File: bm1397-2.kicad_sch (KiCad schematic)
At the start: 101 parts, among them IC1 BM1397_mode1, J3 Conn_01x05, U3 SN74LVC1T45DBVR, U5 MCP1824T-1802E, U5 SN74LVC1T45DBVR, U6 MCP1824T-0802E, U8 SN74LVC1T45DBVR, X1 OT322525MJBA4SL

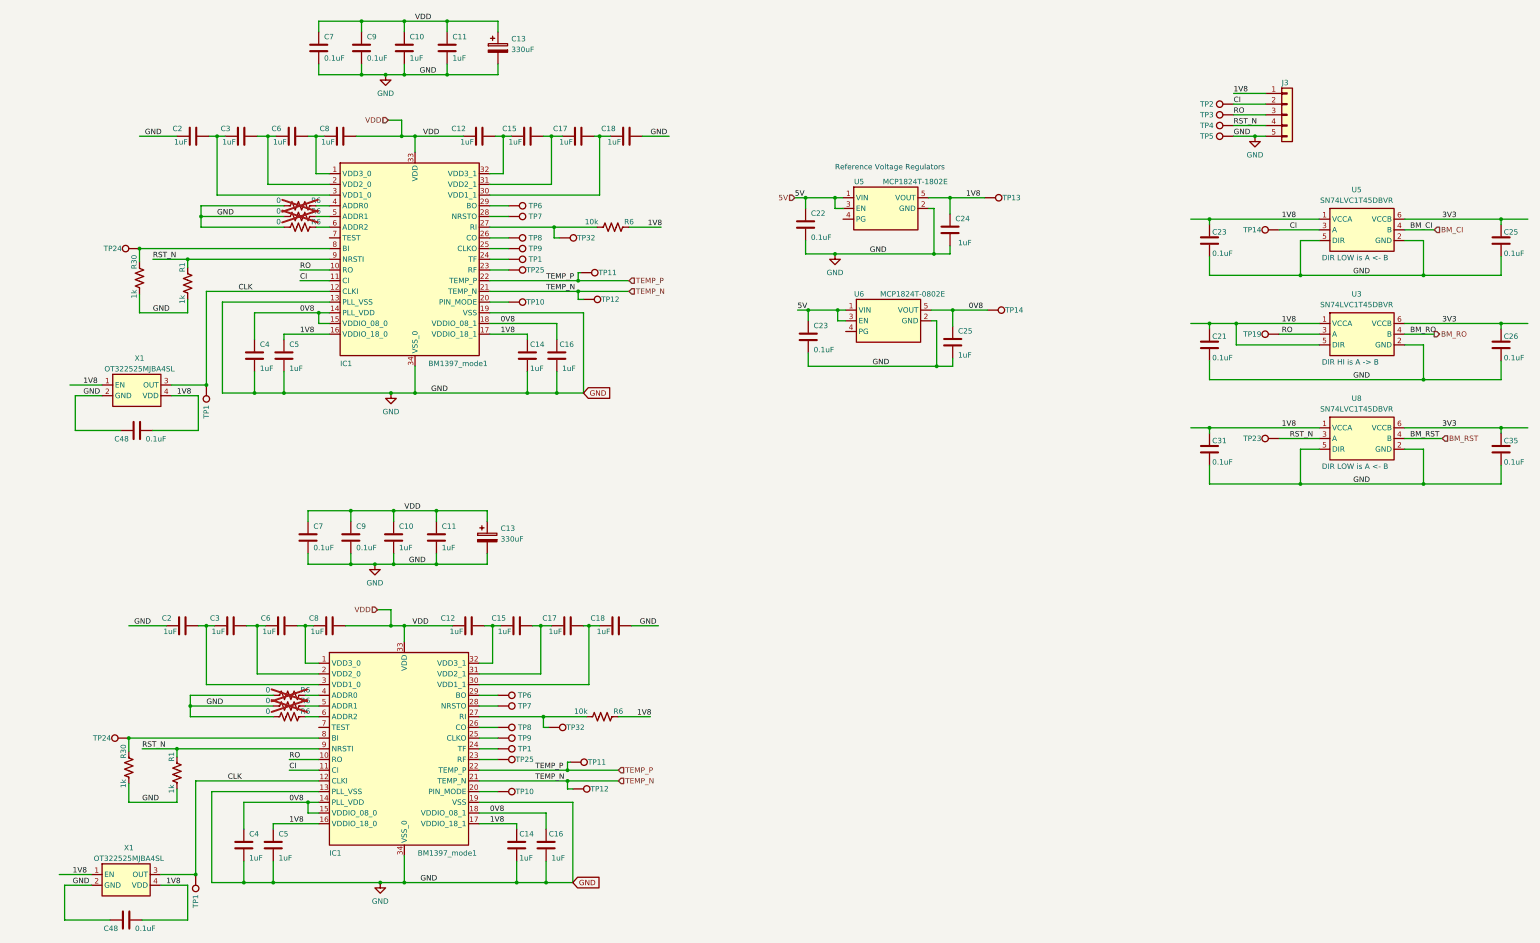
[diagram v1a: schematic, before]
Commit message: starting to sort out the asic data connections
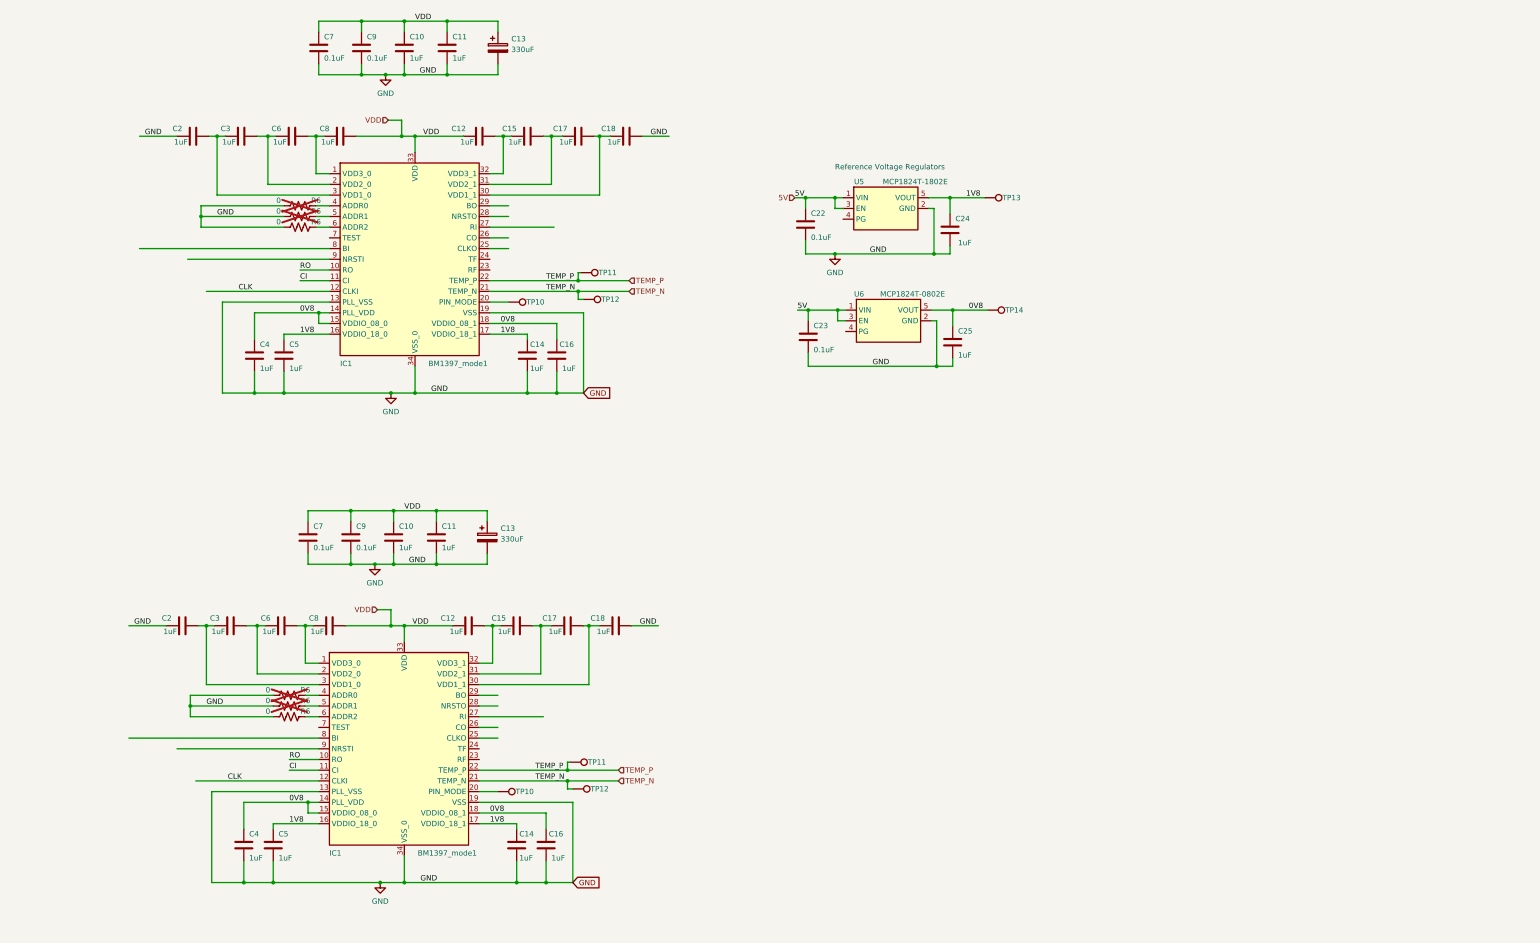
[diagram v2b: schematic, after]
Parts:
- removed C21, C23, C25, C26, C31, C35, C48 (x2): 311-3342-1-ND, Capacitor_SMD:C_0402_1005Metric, symbol Device:C
- removed J3: Conn_01x05, Connector_PinHeader_2.54mm:PinHeader_1x05_P2.54mm_Vertical, symbol Connector_Generic:Conn_01x05
- removed R1 (x2), R30 (x2): 1k, Resistor_SMD:R_0402_1005Metric, symbol Device:R_US
- removed R6 (x2): 10k, Resistor_SMD:R_0402_1005Metric, symbol Device:R_US
- removed TP1 (x4), TP14, TP19, TP2, TP23, TP24 (x2), TP25 (x2), TP3, TP32 (x2), TP4, TP5, TP6 (x2), TP7 (x2), TP8 (x2), TP9 (x2): TestPoint, TestPoint:TestPoint_Pad_D1.5mm, symbol Connector:TestPoint
- removed U3, U5, U8: SN74LVC1T45DBVR, lcsc:SOT-23-6_L2.9-W1.6-P0.95-LS2.8-BR, symbol lcsc:SN74LVC1T45DBVR
- removed X1 (x2): OT322525MJBA4SL, lcsc:OSC-SMD_4P-L3.2-W2.5-BL, symbol lcsc:OT322525MJBA4SL
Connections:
- net RST_N: no longer names the net of IC1.9 (NRSTI)
- net RST_N: no longer IC1.9 (NRSTI)
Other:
- note removed: "DIR HI is A -> B"
- note removed: "DIR LOW is A <- B"

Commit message: connected up power and data to ASICs in schematic
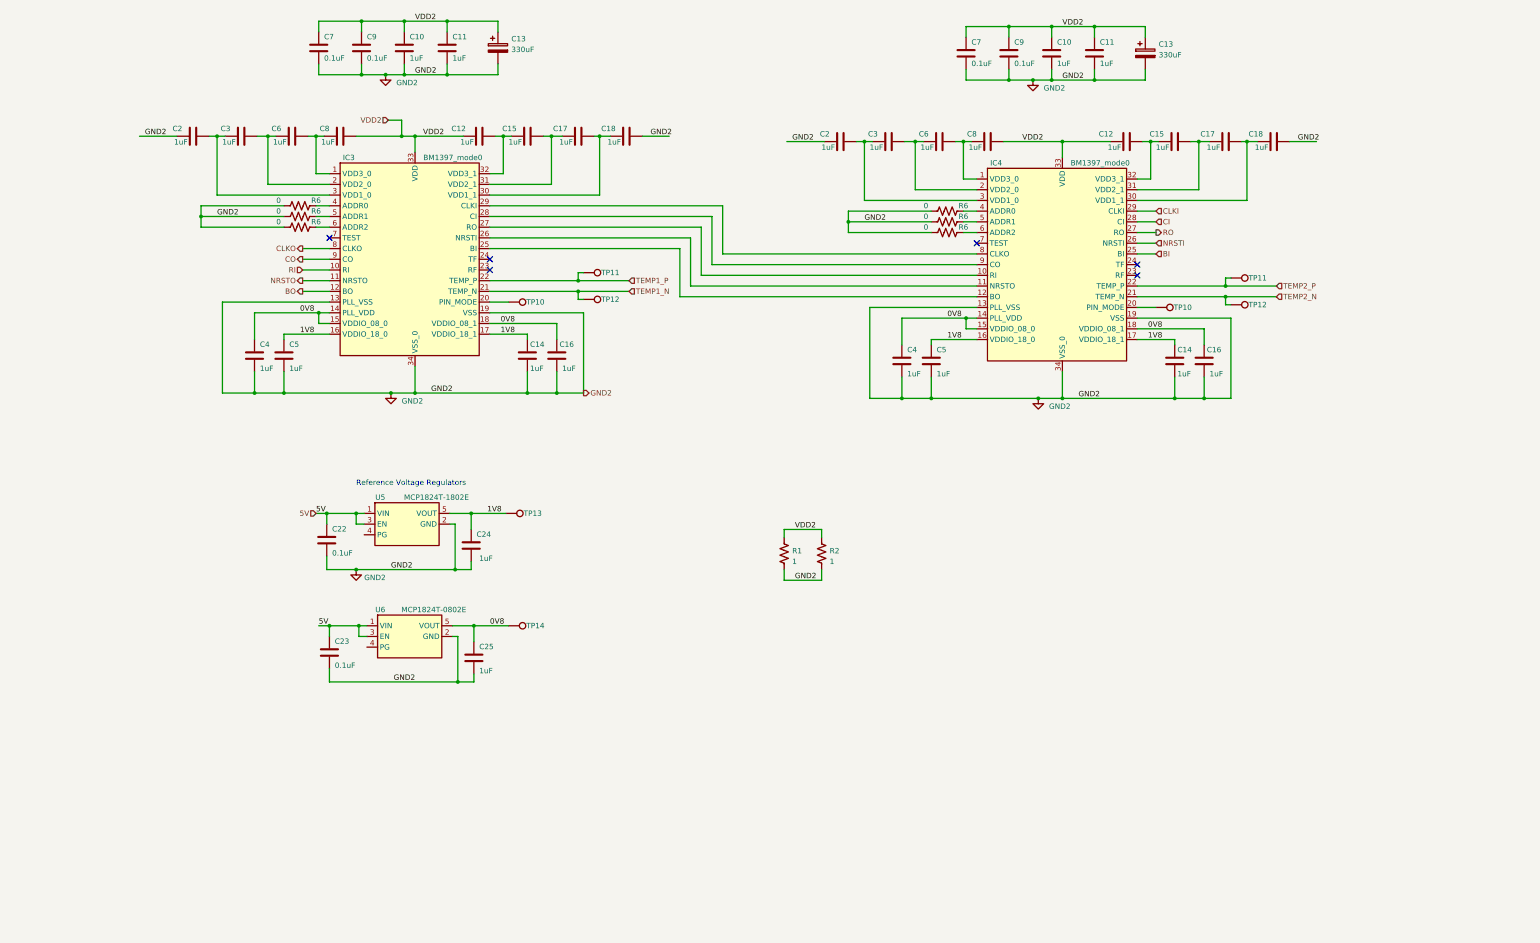
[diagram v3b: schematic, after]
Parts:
- removed IC1 (x2): BM1397_mode1, bitaxe:BM1397, symbol bitaxe:BM1397_mode1
- added IC3, IC4: BM1397_mode0, symbol Bitaxe:BM1397_mode0
- added R1, R2: 1, Resistor_SMD:R_2512_6332Metric, symbol Device:R_US
- R6: now fitted
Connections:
- net 0V8: now also IC3.14 (PLL_VDD), IC3.15 (VDDIO_08_0), IC3.18 (VDDIO_08_1), IC4.14 (PLL_VDD), IC4.15 (VDDIO_08_0), IC4.18 (VDDIO_08_1)
- net 1V8: now also IC3.16 (VDDIO_18_0), IC3.17 (VDDIO_18_1), IC4.16 (VDDIO_18_0), IC4.17 (VDDIO_18_1)
- net CI: now also IC4.28 (CI)
- net GND: now also IC3.13 (PLL_VSS), IC3.19 (VSS), IC3.34 (VSS_0), IC4.13 (PLL_VSS), IC4.19 (VSS), IC4.34 (VSS_0), R1.2, R2.2
- net RO: now also IC4.27 (RO)
- net at C12.2, C15.1: now also IC3.32 (VDD3_1)
- net at C15.2, C17.1: now also IC3.31 (VDD2_1)
- net at C17.2, C18.1: now also IC3.30 (VDD1_1)
- net at C15.2, C17.1: now also IC4.31 (VDD2_1)
- net at C17.2, C18.1: now also IC4.30 (VDD1_1)
- net at TP10.1: now also IC4.20 (PIN_MODE)
- net at C6.2, C8.1: now also IC3.1 (VDD3_0)
- net at C3.2, C6.1: now also IC3.2 (VDD2_0)
- net at TP10.1: now also IC3.20 (PIN_MODE)
- net at C2.2, C3.1: now also IC3.3 (VDD1_0)
- net at R6.2: now also IC3.4 (ADDR0)
- net at R6.2: now also IC3.5 (ADDR1)
- net at R6.2: now also IC3.6 (ADDR2)
- net at C3.2, C6.1: now also IC4.2 (VDD2_0)
- net at C6.2, C8.1: now also IC4.1 (VDD3_0)
- net at C12.2, C15.1: now also IC4.32 (VDD3_1)
- net at C2.2, C3.1: now also IC4.3 (VDD1_0)
- net at R6.2: now also IC4.4 (ADDR0)
- net at R6.2: now also IC4.5 (ADDR1)
- net at R6.2: now also IC4.6 (ADDR2)
- net TEMP_N renamed TEMP1_N
- net TEMP1_N: now also IC3.21 (TEMP_N); no longer TP12.1
- net TEMP_P renamed TEMP1_P
- net TEMP1_P: now also IC3.22 (TEMP_P); no longer TP11.1
- net VDD renamed VDD2
- net VDD2: now also IC3.33 (VDD), IC4.33 (VDD), R1.1, R2.1
- new net: IC3.27 (RO), IC4.10 (RI)
- new net: IC3.26 (NRSTI), IC4.11 (NRSTO)
- new net: IC3.25 (BI), IC4.12 (BO)
- new net: IC3.29 (CLKI), IC4.8 (CLKO)
- new net: IC3.28 (CI), IC4.9 (CO)
- new net BI: IC4.25 (BI)
- new net BO: IC3.12 (BO)
- new net CLKI: IC4.29 (CLKI)
- new net CLKO: IC3.8 (CLKO)
- new net CO: IC3.9 (CO)
- new net NRSTI: IC4.26 (NRSTI)
- new net NRSTO: IC3.11 (NRSTO)
- new net RI: IC3.10 (RI)
- new net TEMP2_N: IC4.21 (TEMP_N), TP12.1
- new net TEMP2_P: IC4.22 (TEMP_P), TP11.1
- no-connect marks 0 -> 6
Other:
- moved on the sheet: C10, C11, C12, C13, C14, C15, C16, C17, C18, C2, C22, C23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

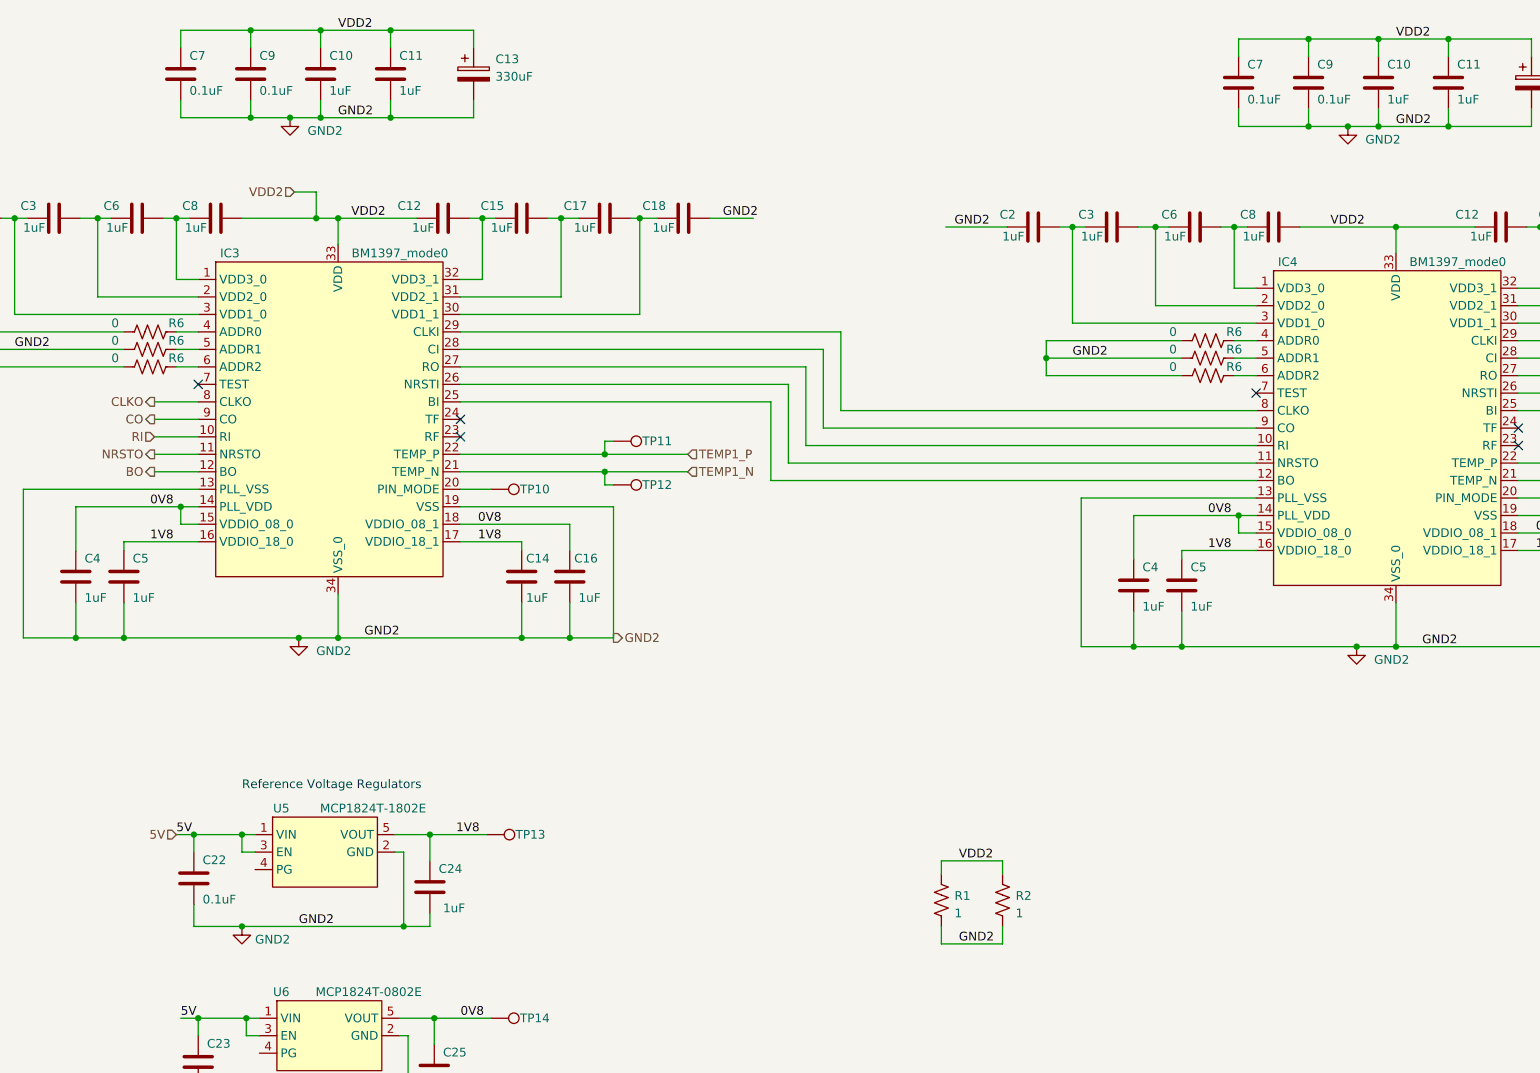
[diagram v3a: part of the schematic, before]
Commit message: fixed the floating gnd net issue. started placement
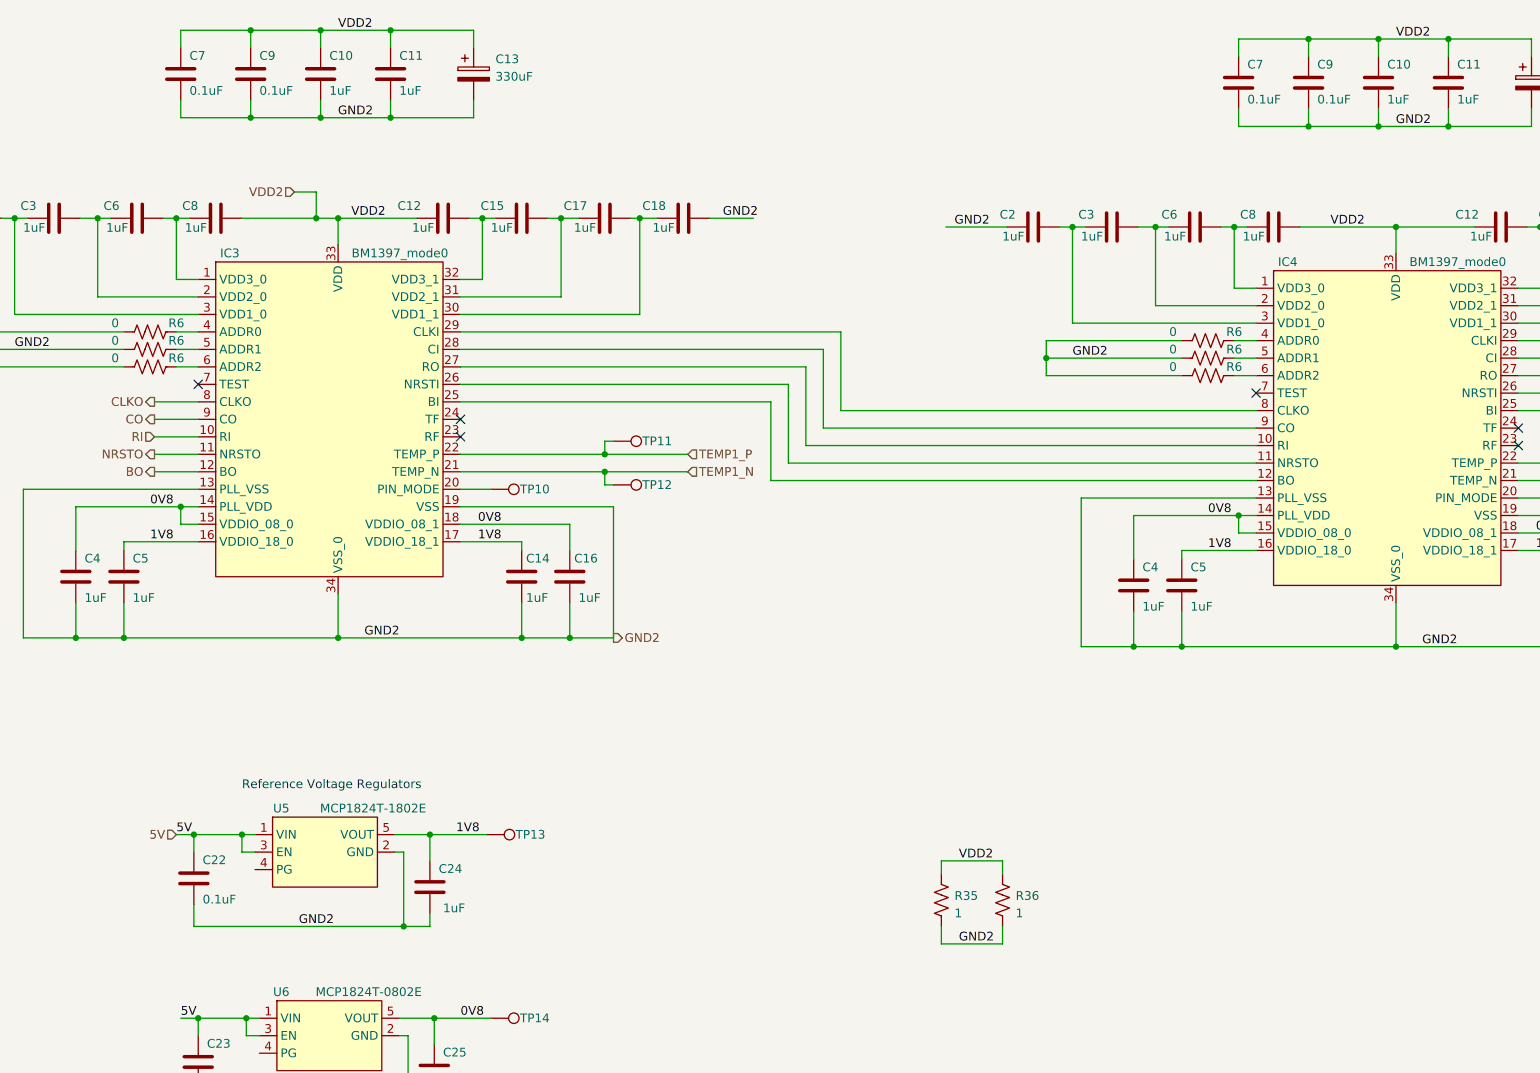
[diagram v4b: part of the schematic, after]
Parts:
- removed C10 (x2), C11 (x2), C12 (x2), C14 (x2), C15 (x2), C16 (x2), C17 (x2), C18 (x2), C2 (x2), C3 (x2), C4 (x2), C5 (x2), C6 (x2), C8 (x2): 587-5514-1-ND, Capacitor_SMD:C_0402_1005Metric, symbol Device:C
- removed C13 (x2): 330uF, Capacitor_Tantalum_SMD:CP_EIA-7343-31_Kemet-D_Pad2.25x2.55mm_HandSolder, symbol Device:C_Polarized
- removed C7 (x2), C9 (x2): 311-3342-1-ND, Capacitor_SMD:C_0402_1005Metric, symbol Device:C
- removed R6 (x6): 0, Resistor_SMD:R_0402_1005Metric, symbol Device:R_US
- added C10 (x2), C11 (x2), C12 (x2), C14 (x2), C15 (x2), C16 (x2), C17 (x2), C18 (x2), C2 (x2), C3 (x2), C4 (x2), C5 (x2), C6 (x2), C8 (x2): 587-5514-1-ND, Capacitor_SMD:C_0402_1005Metric, symbol Device:C
- added C13 (x2): 330uF, Capacitor_Tantalum_SMD:CP_EIA-7343-31_Kemet-D_Pad2.25x2.55mm_HandSolder, symbol Device:C_Polarized
- added C7 (x2), C9 (x2): 311-3342-1-ND, Capacitor_SMD:C_0402_1005Metric, symbol Device:C
- added R6 (x6): 0, Resistor_SMD:R_0402_1005Metric, symbol Device:R_US
- IC3, IC4: footprint (none) -> bitaxe:BM1397
- renumbered R1 to R35, R2 to R36
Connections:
- net 0V8: now also C16.1, C16.1, C4.1, C4.1
- net 1V8: now also C14.1, C14.1, C5.1, C5.1
- net VDD2: now also C10.1, C10.1, C11.1, C11.1, C12.1, C12.1, C13.1, C13.1, C7.1, C7.1, C8.2, C8.2, C9.1, C9.1
- net at IC3.32 (VDD3_1): now also C12.2, C15.1
- net at IC3.31 (VDD2_1): now also C15.2, C17.1
- net at IC3.30 (VDD1_1): now also C17.2, C18.1
- net at IC4.31 (VDD2_1): now also C15.2, C17.1
- net at IC4.30 (VDD1_1): now also C17.2, C18.1
- net at IC3.1 (VDD3_0): now also C6.2, C8.1
- net at IC4.2 (VDD2_0): now also C3.2, C6.1
- net at IC4.1 (VDD3_0): now also C6.2, C8.1
- net at IC3.3 (VDD1_0): now also C2.2, C3.1
- net at IC3.2 (VDD2_0): now also C3.2, C6.1
- net at IC4.32 (VDD3_1): now also C12.2, C15.1
- net at IC4.3 (VDD1_0): now also C2.2, C3.1
- net at IC4.4 (ADDR0): now also R6.2
- net at IC4.5 (ADDR1): now also R6.2
- net at IC4.6 (ADDR2): now also R6.2
- net at IC3.6 (ADDR2): now also R6.2
- net at IC3.4 (ADDR0): now also R6.2
- net at IC3.5 (ADDR1): now also R6.2
- net GND renamed GND2
- net GND2: now also C10.2, C10.2, C11.2, C11.2, C13.2, C13.2, C14.2, C14.2, C16.2, C16.2, C18.2, C18.2, C2.1, C2.1, C4.2, C4.2, C5.2, C5.2, C7.2, C7.2, C9.2, C9.2, R6.1, R6.1, R6.1, R6.1, R6.1, R6.1
